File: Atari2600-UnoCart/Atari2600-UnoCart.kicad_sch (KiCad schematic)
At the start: 22 parts, among them J1 A2600 card edge, J2 Micro_SD_Card, J3 PROG, U1 STM32F407VGTx, U2 SPX3819M5-L-3-3, U3 XC6206PxxxMR

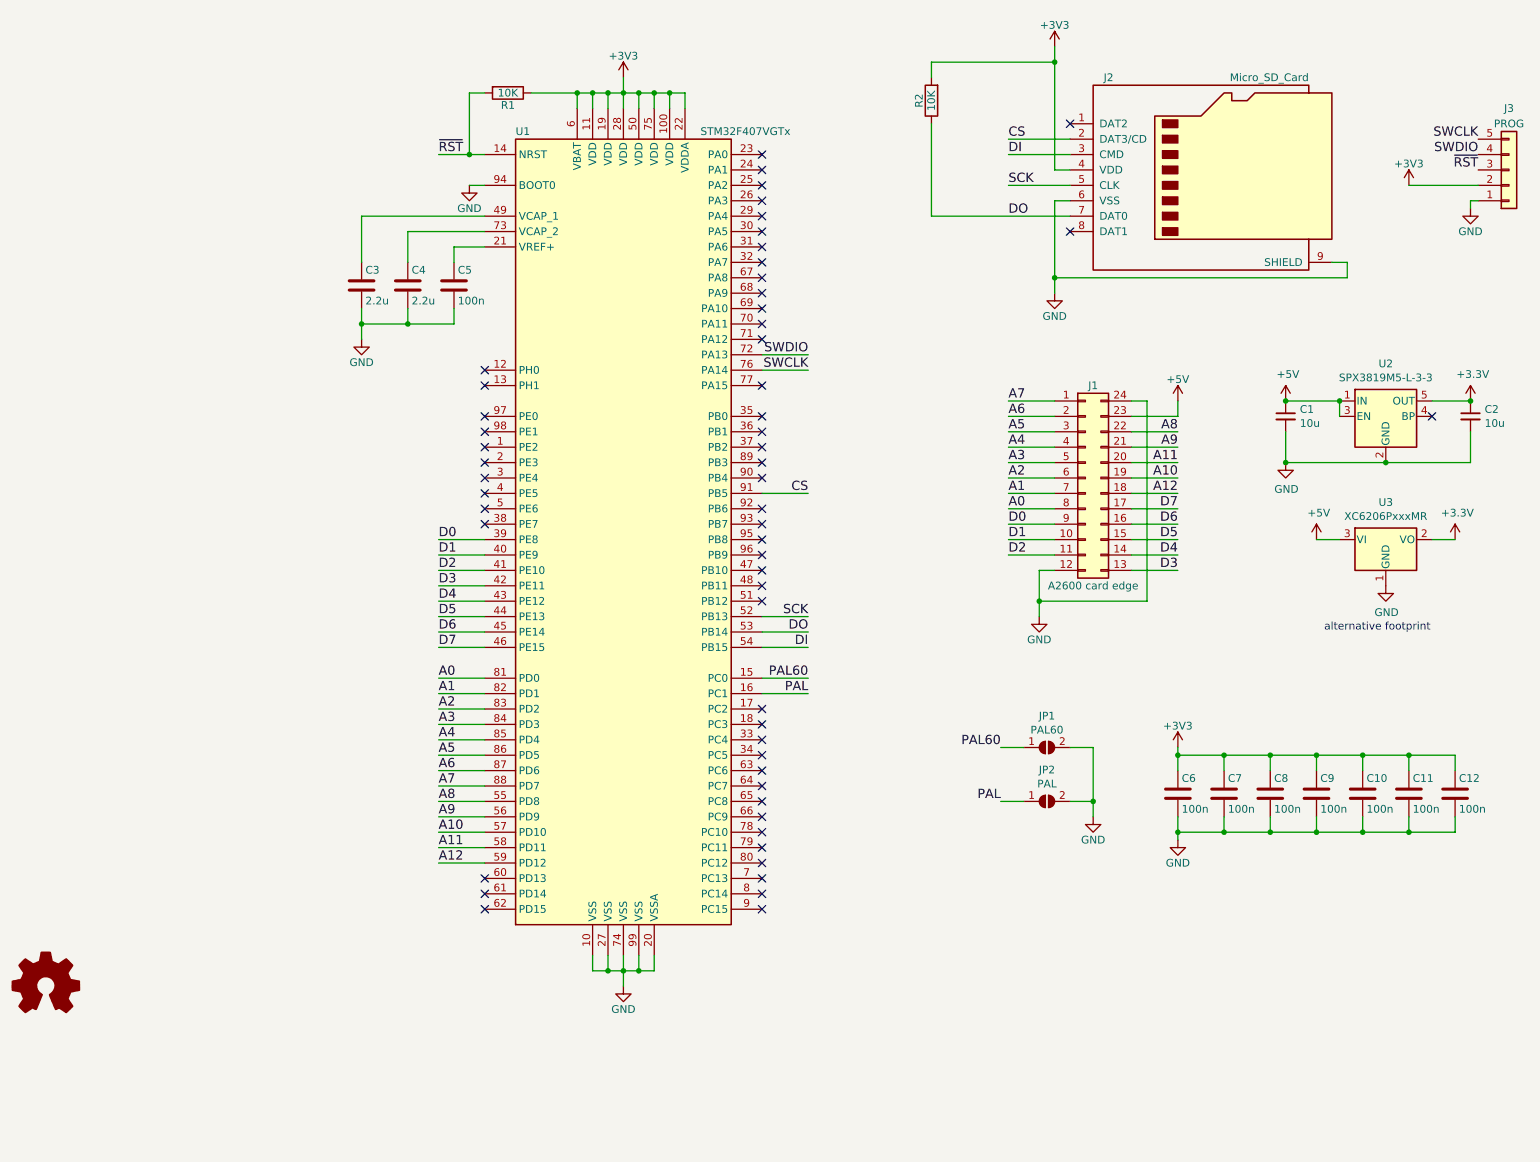
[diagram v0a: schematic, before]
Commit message: Addition of Atari2600-SECAM2RGB ; update license of Atari2600-UnoCart and README.
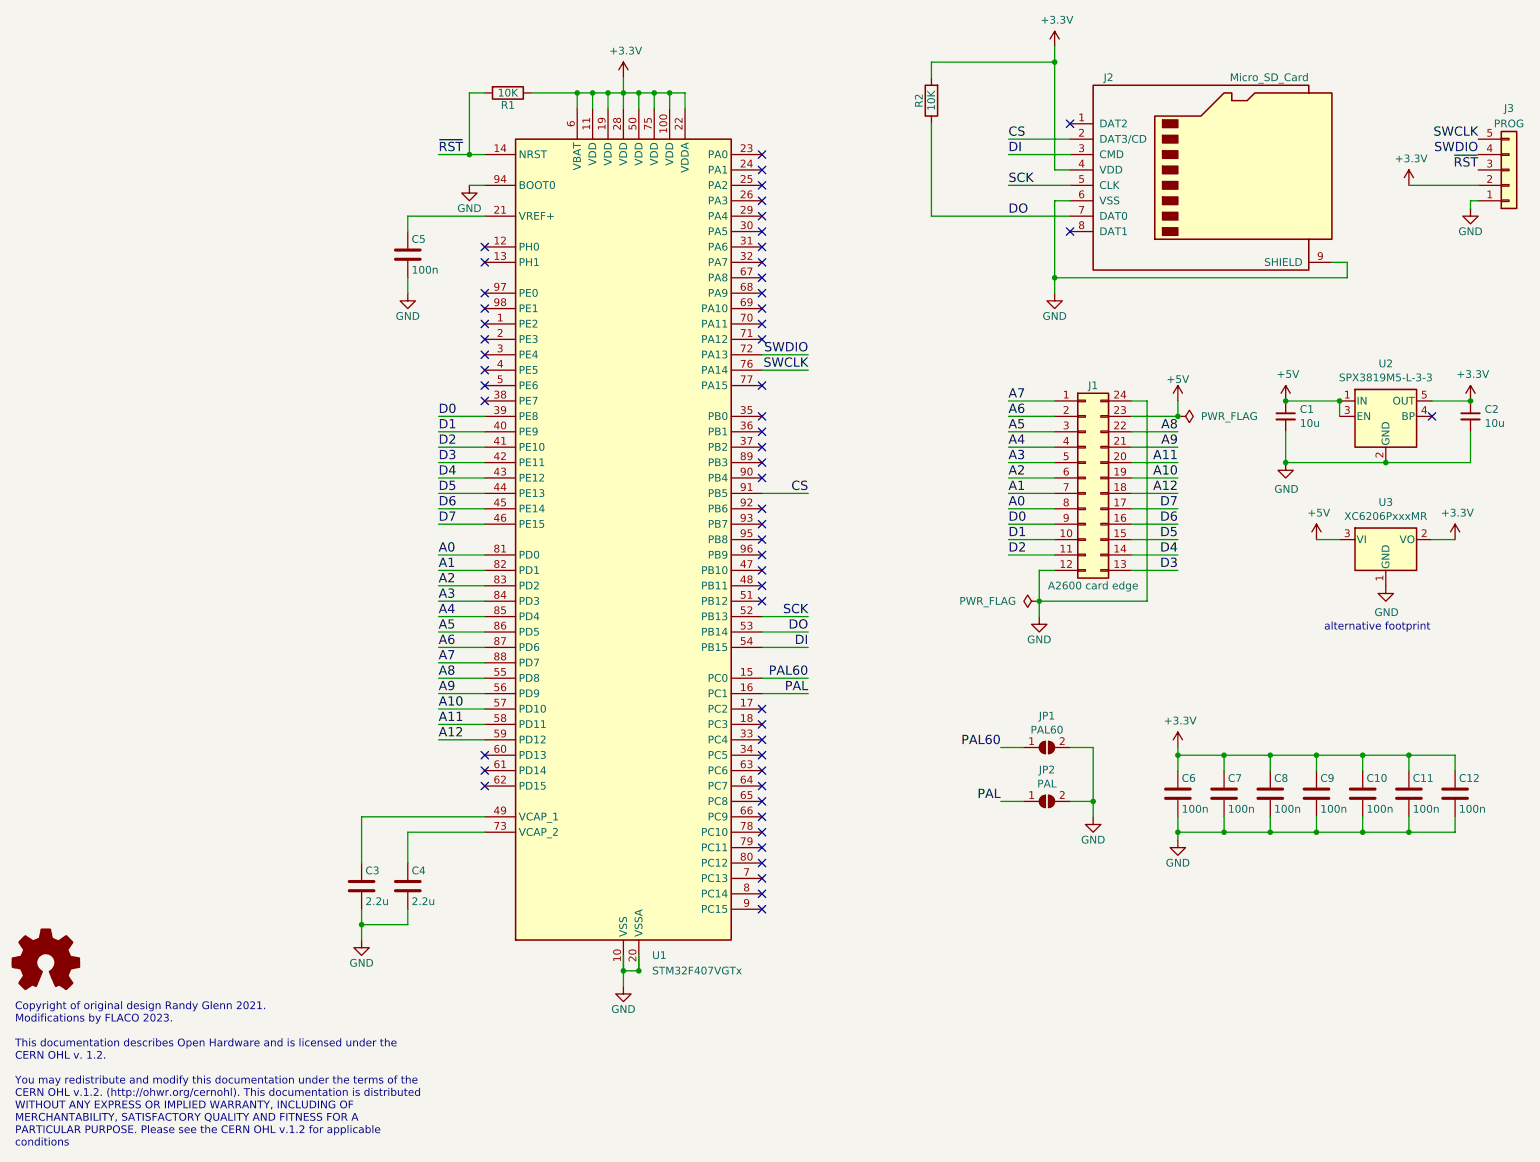
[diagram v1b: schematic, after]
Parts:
- removed U1: STM32F407VGTx, Package_QFP:LQFP-100_14x14mm_P0.5mm, symbol MCU_ST_STM32F41:STM32F407VGTx
- added U1: STM32F407VGTx, Package_QFP:LQFP-100_14x14mm_P0.5mm, symbol MCU_ST_STM32F4:STM32F407VGTx
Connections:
- net A0: now also U1.81 (PD0)
- net A1: now also U1.82 (PD1)
- net A10: now also U1.57 (PD10)
- net A11: now also U1.58 (PD11)
- net A12: now also U1.59 (PD12)
- net A2: now also U1.83 (PD2)
- net A3: now also U1.84 (PD3)
- net A4: now also U1.85 (PD4)
- net A5: now also U1.86 (PD5)
- net A6: now also U1.87 (PD6)
- net A7: now also U1.88 (PD7)
- net A8: now also U1.55 (PD8)
- net A9: now also U1.56 (PD9)
- net CS: now also U1.91 (PB5)
- net D0: now also U1.39 (PE8)
- net D1: now also U1.40 (PE9)
- net D2: now also U1.41 (PE10)
- net D3: now also U1.42 (PE11)
- net D4: now also U1.43 (PE12)
- net D5: now also U1.44 (PE13)
- net D6: now also U1.45 (PE14)
- net D7: now also U1.46 (PE15)
- net DI: now also U1.54 (PB15)
- net DO: now also U1.53 (PB14)
- net GND: now also U1.10 (VSS), U1.20 (VSSA), U1.27 (VSS), U1.74 (VSS), U1.94 (BOOT0), U1.99 (VSS)
- net PAL: now also U1.16 (PC1)
- net PAL60: now also U1.15 (PC0)
- net SCK: now also U1.52 (PB13)
- net SWCLK: now also U1.76 (PA14)
- net SWDIO: now also U1.72 (PA13)
- net ~{RST}: now also U1.14 (NRST)
- net at C5.1: now also U1.21 (VREF+)
- net at C3.1: now also U1.49 (VCAP_1)
- net at C4.1: now also U1.73 (VCAP_2)
- net +3V3 renamed +3.3V
- net +3.3V: now also U1.100 (VDD), U1.11 (VDD), U1.19 (VDD), U1.22 (VDDA), U1.28 (VDD), U1.50 (VDD), U1.6 (VBAT), U1.75 (VDD)
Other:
- note added: "Copyright of original design Randy Glenn 2021. Modifications by FLACO 2023. This documentation describes Open Hardware and is licensed under the CERN OHL v. 1.2. You may redistribute and modify this documentation under the terms of the CERN OHL v.1.2. (http://ohwr.org/cernohl). This documentation is distributed WITHOUT ANY EXPRESS OR IMPLIED WARRANTY, INCLUDING OF MERCHANTABILITY, SATISFACTORY QU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"
- moved on the sheet: C3, C4, C5
